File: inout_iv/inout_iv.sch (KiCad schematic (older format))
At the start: 1 part, among them P1 DIN_41612_128P

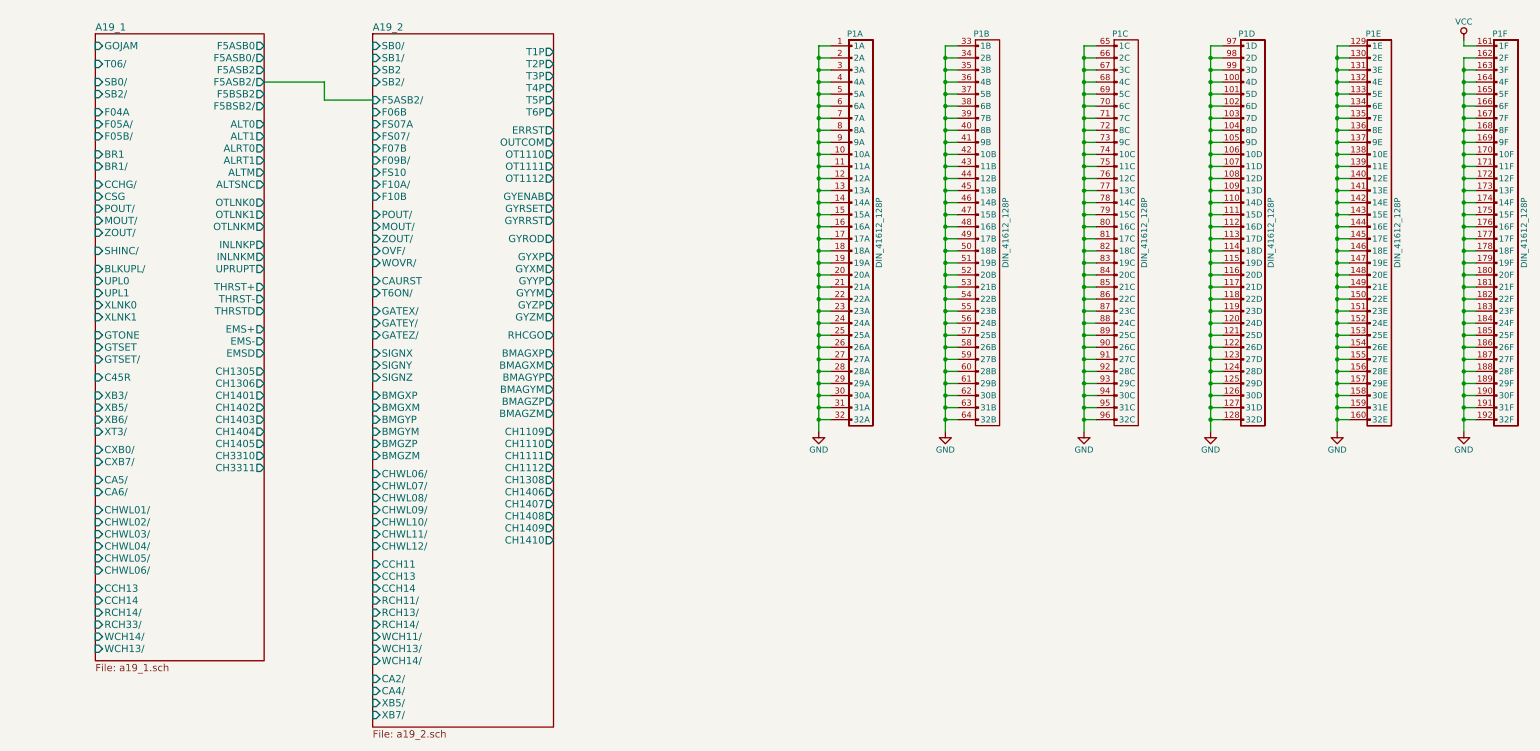
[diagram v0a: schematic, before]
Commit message: Tied in Inout IV and renamed MONPCH to the original MON+CH
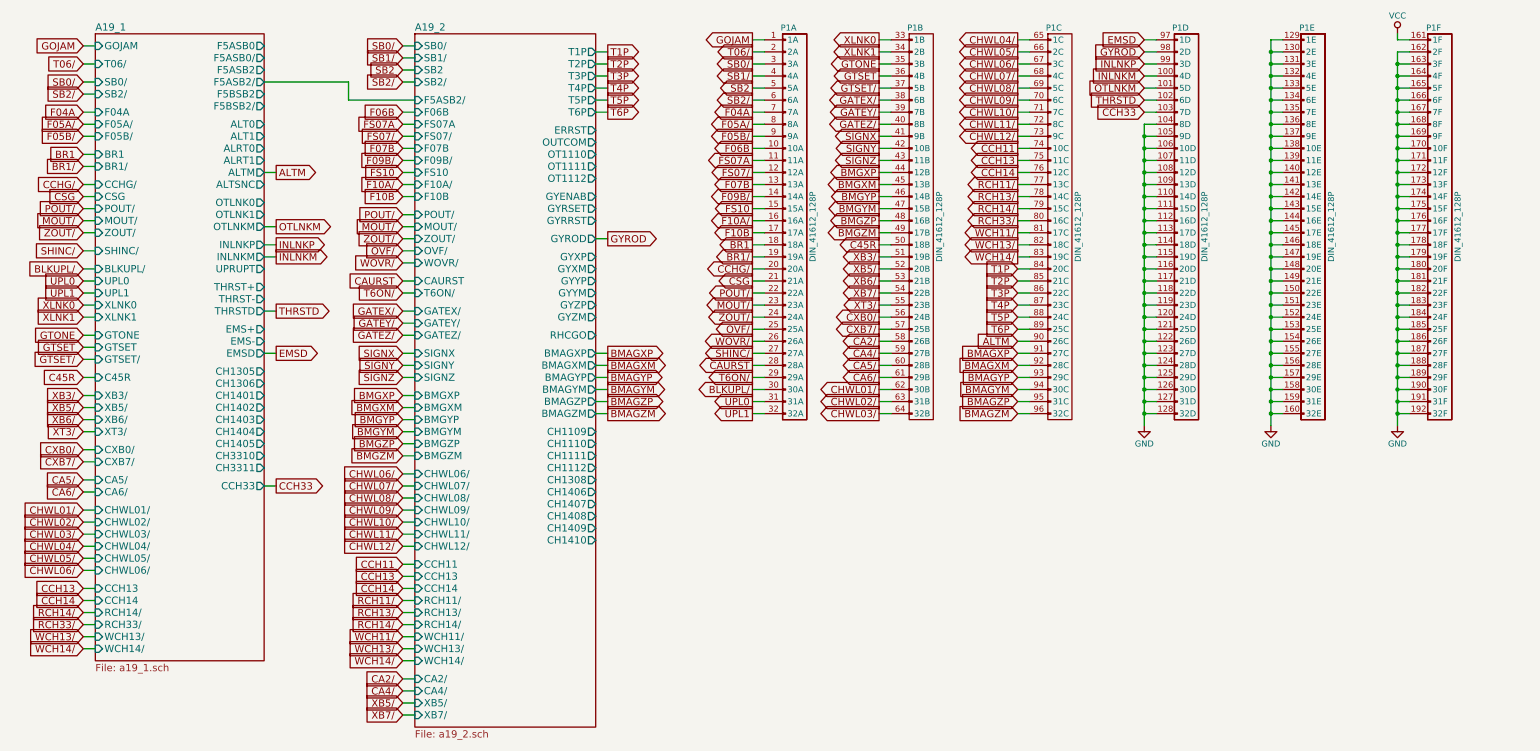
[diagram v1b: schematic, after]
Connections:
- net GND: no longer P1.1 (1A), P1.10 (10A), P1.100 (4D), P1.101 (5D), P1.102 (6D), P1.103 (7D), P1.11 (11A), P1.12 (12A), P1.13 (13A), P1.14 (14A), P1.15 (15A), P1.16 (16A), P1.17 (17A), P1.18 (18A), P1.19 (19A), P1.2 (2A), P1.20 (20A), P1.21 (21A), P1.22 (22A), P1.23 (23A), P1.24 (24A), P1.25 (25A), P1.26 (26A), P1.27 (27A), P1.28 (28A), P1.29 (29A), P1.3 (3A), P1.30 (30A), P1.31 (31A), P1.32 (32A), P1.33 (1B), P1.34 (2B), P1.35 (3B), P1.36 (4B), P1.37 (5B), P1.38 (6B), P1.39 (7B), P1.4 (4A), P1.40 (8B), P1.41 (9B), P1.42 (10B), P1.43 (11B), P1.44 (12B), P1.45 (13B), P1.46 (14B), P1.47 (15B), P1.48 (16B), P1.49 (17B), P1.5 (5A), P1.50 (18B), P1.51 (19B), P1.52 (20B), P1.53 (21B), P1.54 (22B), P1.55 (23B), P1.56 (24B), P1.57 (25B), P1.58 (26B), P1.59 (27B), P1.6 (6A), P1.60 (28B), P1.61 (29B), P1.62 (30B), P1.63 (31B), P1.64 (32B), P1.65 (1C), P1.66 (2C), P1.67 (3C), P1.68 (4C), P1.69 (5C), P1.7 (7A), P1.70 (6C), P1.71 (7C), P1.72 (8C), P1.73 (9C), P1.74 (10C), P1.75 (11C), P1.76 (12C), P1.77 (13C), P1.78 (14C), P1.79 (15C), P1.8 (8A), P1.80 (16C), P1.81 (17C), P1.82 (18C), P1.83 (19C), P1.84 (20C), P1.85 (21C), P1.86 (22C), P1.87 (23C), P1.88 (24C), P1.89 (25C), P1.9 (9A), P1.90 (26C), P1.91 (27C), P1.92 (28C), P1.93 (29C), P1.94 (30C), P1.95 (31C), P1.96 (32C), P1.97 (1D), P1.98 (2D), P1.99 (3D)
- new net ALTM: P1.90 (26C)
- new net BLKUPL/: P1.30 (30A)
- new net BMAGXM: P1.92 (28C)
- new net BMAGXP: P1.91 (27C)
- new net BMAGYM: P1.94 (30C)
- new net BMAGYP: P1.93 (29C)
- new net BMAGZM: P1.96 (32C)
- new net BMAGZP: P1.95 (31C)
- new net BMGXM: P1.45 (13B)
- new net BMGXP: P1.44 (12B)
- new net BMGYM: P1.47 (15B)
- new net BMGYP: P1.46 (14B)
- new net BMGZM: P1.49 (17B)
- new net BMGZP: P1.48 (16B)
- new net BR1: P1.18 (18A)
- new net BR1/: P1.19 (19A)
- new net C45R: P1.50 (18B)
- new net CA2/: P1.58 (26B)
- new net CA4/: P1.59 (27B)
- new net CA5/: P1.60 (28B)
- new net CA6/: P1.61 (29B)
- new net CAURST: P1.28 (28A)
- new net CCH11: P1.74 (10C)
- new net CCH13: P1.75 (11C)
- new net CCH14: P1.76 (12C)
- new net CCH33: P1.103 (7D)
- new net CCHG/: P1.20 (20A)
- new net CHWL01/: P1.62 (30B)
- new net CHWL02/: P1.63 (31B)
- new net CHWL03/: P1.64 (32B)
- new net CHWL04/: P1.65 (1C)
- new net CHWL05/: P1.66 (2C)
- new net CHWL06/: P1.67 (3C)
- new net CHWL07/: P1.68 (4C)
- new net CHWL08/: P1.69 (5C)
- new net CHWL09/: P1.70 (6C)
- new net CHWL10/: P1.71 (7C)
- new net CHWL11/: P1.72 (8C)
- new net CHWL12/: P1.73 (9C)
- new net CSG: P1.21 (21A)
- new net CXB0/: P1.56 (24B)
- new net CXB7/: P1.57 (25B)
- new net EMSD: P1.97 (1D)
- new net F04A: P1.7 (7A)
- new net F05A/: P1.8 (8A)
- new net F05B/: P1.9 (9A)
- new net F06B: P1.10 (10A)
- new net F07B: P1.13 (13A)
- new net F09B/: P1.14 (14A)
- new net F10A/: P1.16 (16A)
- new net F10B: P1.17 (17A)
- new net FS07/: P1.12 (12A)
- new net FS07A: P1.11 (11A)
- new net FS10: P1.15 (15A)
- new net GATEX/: P1.38 (6B)
- new net GATEY/: P1.39 (7B)
- new net GATEZ/: P1.40 (8B)
- new net GOJAM: P1.1 (1A)
- new net GTONE: P1.35 (3B)
- new net GTSET: P1.36 (4B)
- new net GTSET/: P1.37 (5B)
- new net GYROD: P1.98 (2D)
- new net INLNKM: P1.100 (4D)
- new net INLNKP: P1.99 (3D)
- new net MOUT/: P1.23 (23A)
- new net OTLNKM: P1.101 (5D)
- new net OVF/: P1.25 (25A)
- new net POUT/: P1.22 (22A)
- new net RCH11/: P1.77 (13C)
- new net RCH13/: P1.78 (14C)
- new net RCH14/: P1.79 (15C)
- new net RCH33/: P1.80 (16C)
- new net SB0/: P1.3 (3A)
- new net SB1/: P1.4 (4A)
- new net SB2: P1.5 (5A)
- new net SB2/: P1.6 (6A)
- new net SHINC/: P1.27 (27A)
- new net SIGNX: P1.41 (9B)
- new net SIGNY: P1.42 (10B)
- new net SIGNZ: P1.43 (11B)
- new net T06/: P1.2 (2A)
- new net T1P: P1.84 (20C)
- new net T2P: P1.85 (21C)
- new net T3P: P1.86 (22C)
- new net T4P: P1.87 (23C)
- new net T5P: P1.88 (24C)
- new net T6ON/: P1.29 (29A)
- new net T6P: P1.89 (25C)
- new net THRSTD: P1.102 (6D)
- new net UPL0: P1.31 (31A)
- new net UPL1: P1.32 (32A)
- new net WCH11/: P1.81 (17C)
- new net WCH13/: P1.82 (18C)
- new net WCH14/: P1.83 (19C)
- new net WOVR/: P1.26 (26A)
- new net XB3/: P1.51 (19B)
- new net XB5/: P1.52 (20B)
- new net XB6/: P1.53 (21B)
- new net XB7/: P1.54 (22B)
- new net XLNK0: P1.33 (1B)
- new net XLNK1: P1.34 (2B)
- new net XT3/: P1.55 (23B)
- new net ZOUT/: P1.24 (24A)
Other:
- moved on the sheet: P1A, P1B, P1C, P1D, P1E, P1F

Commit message: Tied in Inout II.
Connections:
- net GND: no longer P1.104 (8D), P1.105 (9D), P1.106 (10D), P1.107 (11D), P1.108 (12D), P1.109 (13D), P1.110 (14D), P1.111 (15D), P1.112 (16D), P1.113 (17D), P1.114 (18D), P1.115 (19D), P1.116 (20D), P1.117 (21D)
- new net CH1305: P1.104 (8D)
- new net CH1306: P1.105 (9D)
- new net CH1308: P1.106 (10D)
- new net CH1401: P1.107 (11D)
- new net CH1402: P1.108 (12D)
- new net CH1403: P1.109 (13D)
- new net CH1404: P1.110 (14D)
- new net CH1405: P1.111 (15D)
- new net CH1406: P1.112 (16D)
- new net CH1407: P1.113 (17D)
- new net CH1408: P1.114 (18D)
- new net CH1409: P1.115 (19D)
- new net CH1410: P1.116 (20D)
- new net CH3310: P1.117 (21D)
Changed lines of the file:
@@
 $EndComp
-Wire Wire Line
-	10500 1950 10600 1950
-Wire Wire Line
-	10500 2050 10600 2050
-Connection ~ 10500 2050
-Wire Wire Line
-	10500 2150 10600 2150
-Connection ~ 10500 2150
-Wire Wire Line
-	10500 2250 10600 2250
-Connection ~ 10500 2250
-Wire Wire Line
-	10500 2350 10600 2350
-Connection ~ 10500 2350
-Wire Wire Line
-	10500 2450 10600 2450
-Connection ~ 10500 2450
-Wire Wire Line
-	10500 2550 10600 2550
-Connection ~ 10500 2550
-Wire Wire Line
-	10500 2650 10600 2650
-Connection ~ 10500 2650
-Wire Wire Line
-	10500 2750 10600 2750
-Connection ~ 10500 2750
-Wire Wire Line
-	10500 2850 10600 2850
-Connection ~ 10500 2850
-Wire Wire Line
-	10500 2950 10600 2950
-Connection ~ 10500 2950
-Wire Wire Line
-	10500 3050 10600 3050
-Connection ~ 10500 3050
-Wire Wire Line
-	10500 3150 10600 3150
-Connection ~ 10500 3150
-Wire Wire Line
-	10500 3250 10600 3250
-Connection ~ 10500 3250
-Wire Wire Line
-	10500 3350 10600 3350
-Connection ~ 10500 3350
-Wire Wire Line
-	10500 3450 10600 3450
-Connection ~ 10500 3450
-Wire Wire Line
-	10500 3550 10600 3550
-Connection ~ 10500 3550
-Wire Wire Line
-	10500 3650 10600 3650
-Connection ~ 10500 3650
-Wire Wire Line
-	10500 3750 10600 3750
-Connection ~ 10500 3750
-Wire Wire Line
-	10500 3850 10600 3850
-Connection ~ 10500 3850
-Wire Wire Line
-	10500 3950 10600 3950
-Connection ~ 10500 3950
 Wire Wire Line
 	10500 4050 10600 4050
@@
 THRSTD
 Wire Wire Line
-	10500 1950 10500 4450
-Wire Wire Line
 	10600 1750 10500 1750
 Text GLabel 10500 1750 0    60   Input ~ 0
 THRSTD
+Wire Wire Line
+	3200 4000 3300 4000
+Text GLabel 3300 4000 2    60   Output ~ 0
+CH1305
+Wire Wire Line
+	3200 4100 3300 4100
+Text GLabel 3300 4100 2    60   Output ~ 0
+CH1306
+Wire Wire Line
+	3200 4200 3300 4200
+Text GLabel 3300 4200 2    60   Output ~ 0
+CH1401
+Wire Wire Line
+	3200 4300 3300 4300
+Text GLabel 3300 4300 2    60   Output ~ 0
+CH1402
+Wire Wire Line
+	3200 4400 3300 4400
+Text GLabel 3300 4400 2    60   Output ~ 0
+CH1403
+Wire Wire Line
+	3200 4500 3300 4500
+Text GLabel 3300 4500 2    60   Output ~ 0
+CH1404
+Wire Wire Line
+	3200 4600 3300 4600
+Text GLabel 3300 4600 2    60   Output ~ 0
+CH1405
+Wire Wire Line
+	3200 4700 3300 4700
+Text GLabel 3300 4700 2    60   Output ~ 0
+CH3310
+Wire Wire Line
+	5950 4900 6050 4900
+Text GLabel 6050 4900 2    60   Output ~ 0
+CH1308
+Wire Wire Line
+	5950 5000 6050 5000
+Text GLabel 6050 5000 2    60   Output ~ 0
+CH1406
+Wire Wire Line
+	5950 5100 6050 5100
+Text GLabel 6050 5100 2    60   Output ~ 0
+CH1407
+Wire Wire Line
+	5950 5200 6050 5200
+Text GLabel 6050 5200 2    60   Output ~ 0
+CH1408
+Wire Wire Line
+	5950 5300 6050 5300
+Text GLabel 6050 5300 2    60   Output ~ 0
+CH1409
+Wire Wire Line
+	5950 5400 6050 5400
+Text GLabel 6050 5400 2    60   Output ~ 0
+CH1410
+Wire Wire Line
+	10600 1950 10500 1950
+Text GLabel 10500 1950 0    60   Input ~ 0
+CH1305
+Wire Wire Line
+	10600 2050 10500 2050
+Text GLabel 10500 2050 0    60   Input ~ 0
+CH1306
+Wire Wire Line
+	10600 2250 10500 2250
+Text GLabel 10500 2250 0    60   Input ~ 0
+CH1401
+Wire Wire Line
+	10600 2350 10500 2350
+Text GLabel 10500 2350 0    60   Input ~ 0
+CH1402
+Wire Wire Line
+	10600 2450 10500 2450
+Text GLabel 10500 2450 0    60   Input ~ 0
+CH1403
+Wire Wire Line
+	10600 2550 10500 2550
+Text GLabel 10500 2550 0    60   Input ~ 0
+CH1404
+Wire Wire Line
+	10600 2650 10500 2650
+Text GLabel 10500 2650 0    60   Input ~ 0
+CH1405
+Wire Wire Line
+	10600 3250 10500 3250
+Text GLabel 10500 3250 0    60   Input ~ 0
+CH3310
+Wire Wire Line
+	10600 2150 10500 2150
+Text GLabel 10500 2150 0    60   Input ~ 0
+CH1308
+Wire Wire Line
+	10600 2750 10500 2750
+Text GLabel 10500 2750 0    60   Input ~ 0
+CH1406
+Wire Wire Line
+	10600 2850 10500 2850
+Text GLabel 10500 2850 0    60   Input ~ 0
+CH1407
+Wire Wire Line
+	10600 2950 10500 2950
+Text GLabel 10500 2950 0    60   Input ~ 0
+CH1408
+Wire Wire Line
+	10600 3050 10500 3050
+Text GLabel 10500 3050 0    60   Input ~ 0
+CH1409
+Wire Wire Line
+	10600 3150 10500 3150
+Text GLabel 10500 3150 0    60   Input ~ 0
+CH1410
+Wire Wire Line
+	10500 3650 10600 3650
+Connection ~ 10500 3650
+Wire Wire Line
+	10500 3750 10600 3750
+Connection ~ 10500 3750
+Wire Wire Line
+	10500 3850 10600 3850
+Connection ~ 10500 3850
+Wire Wire Line
+	10500 3950 10600 3950
+Connection ~ 10500 3950
+Wire Wire Line
+	10500 3450 10600 3450
+Connection ~ 10500 3450
+Wire Wire Line
+	10500 3550 10600 3550
+Connection ~ 10500 3550
+Wire Wire Line
+	10600 3350 10500 3350
+Wire Wire Line
+	10500 3350 10500 4450
 $EndSCHEMATC

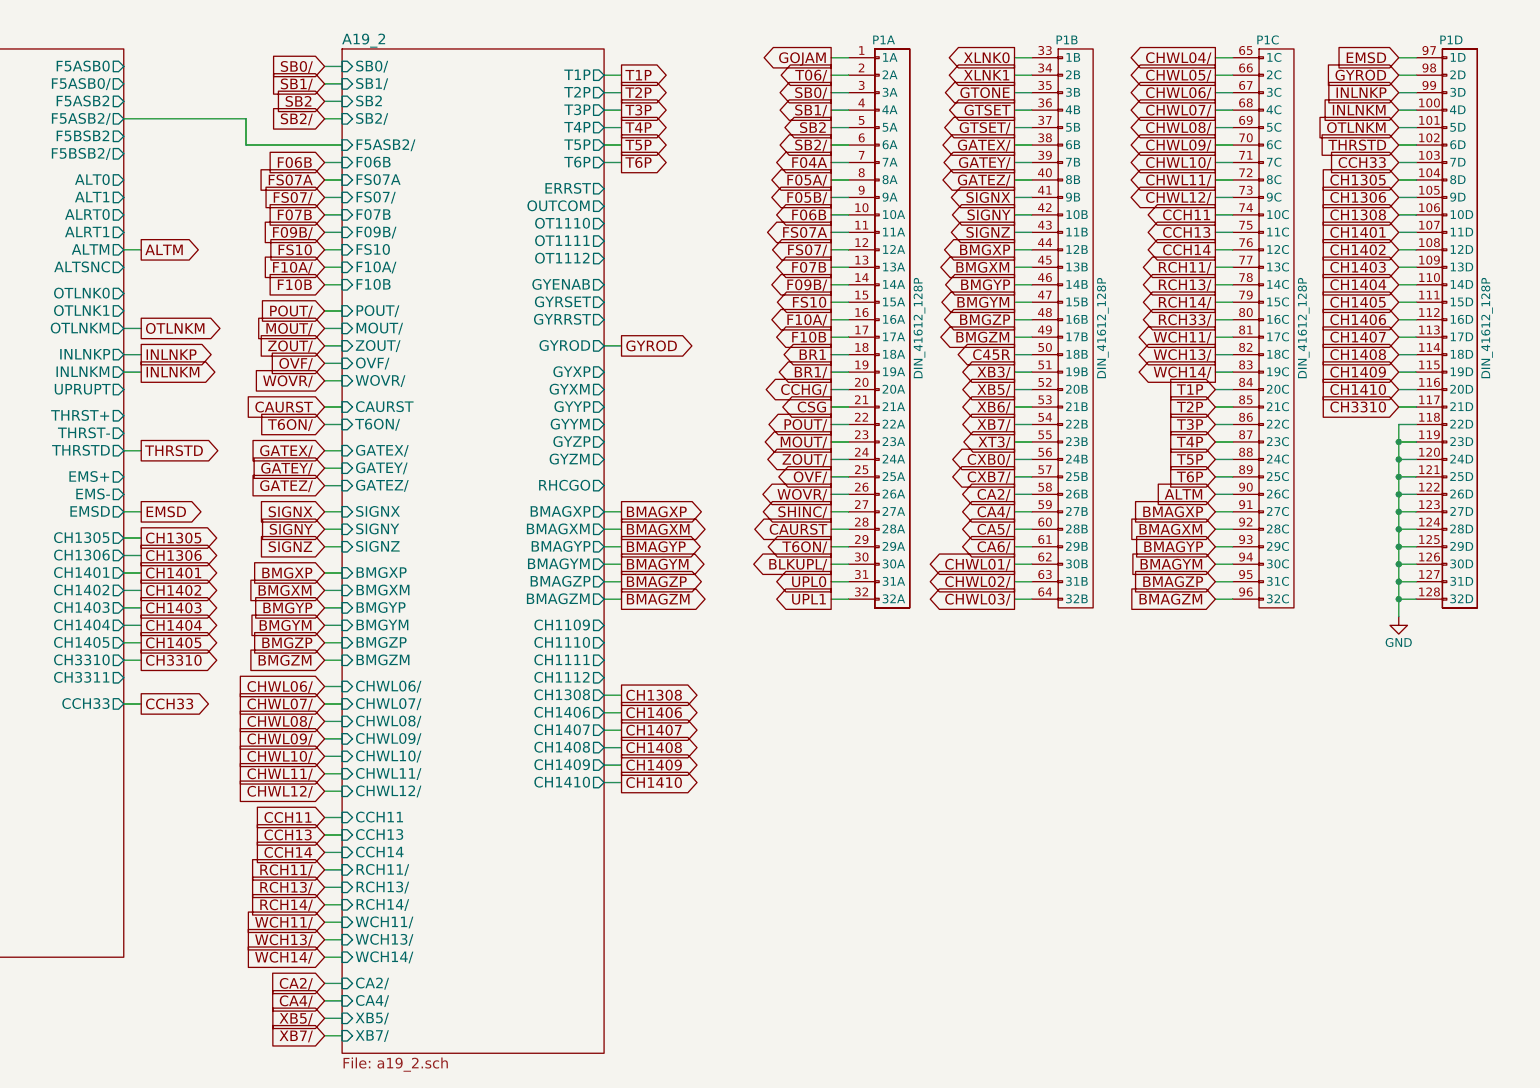
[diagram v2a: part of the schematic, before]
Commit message: Added most of the rest of Inout III and tied it in. Still not sure where to put the downlink stuff, standby, and CHOR propers.
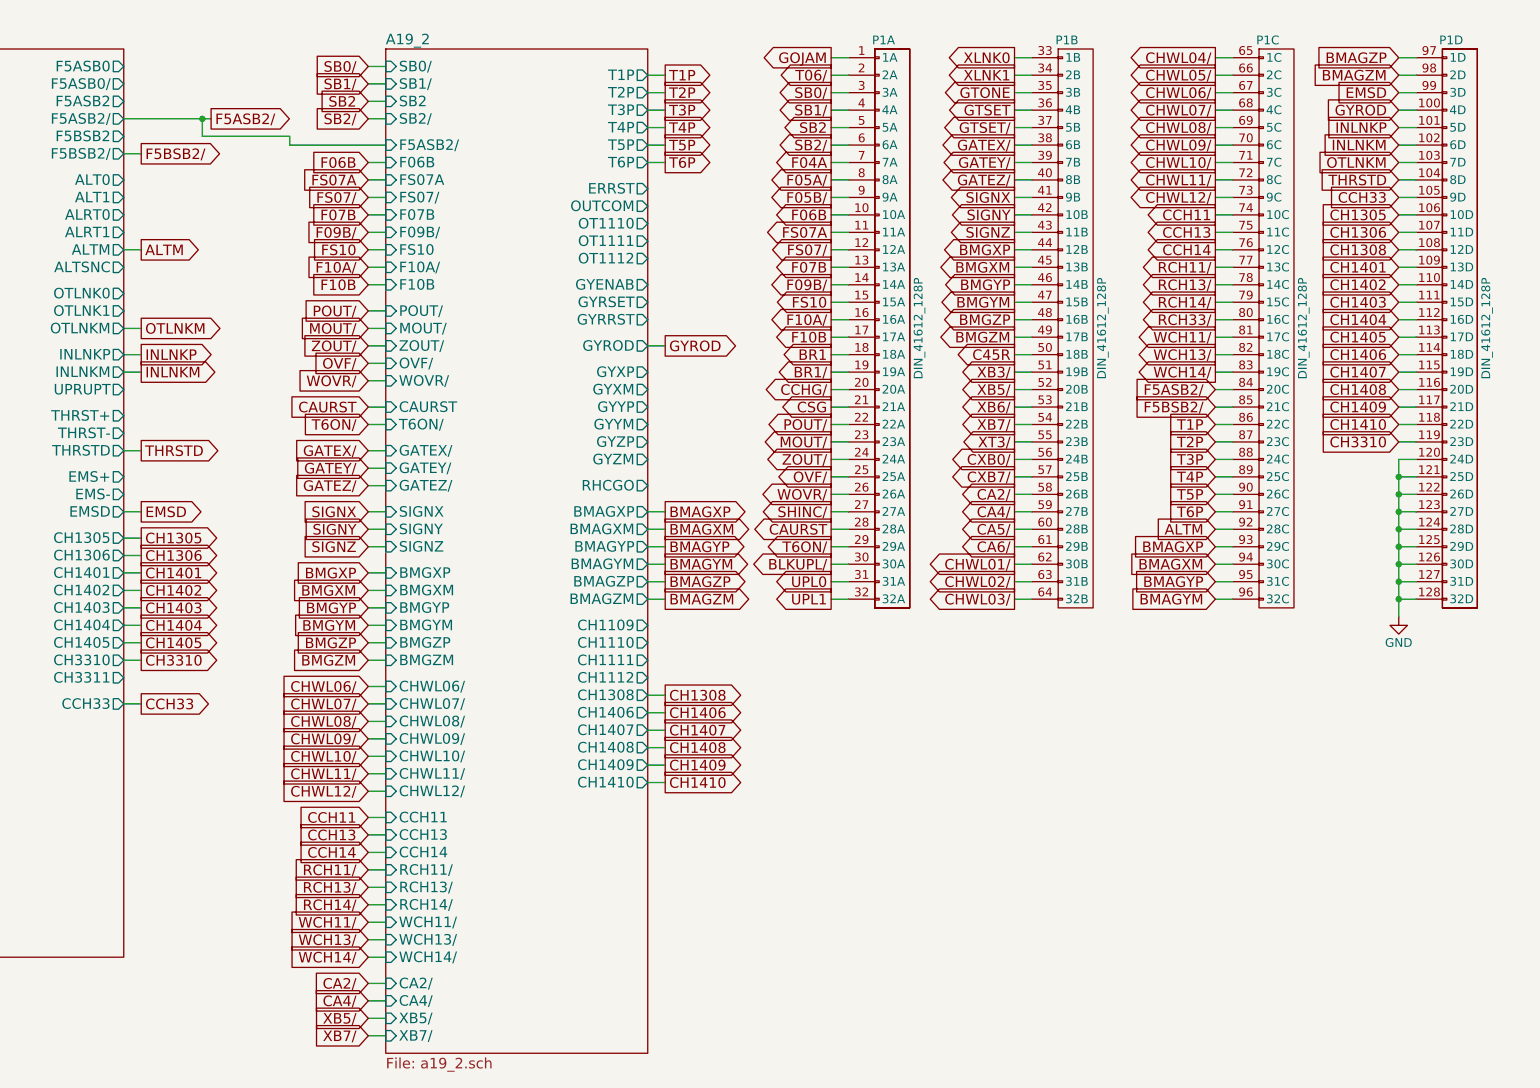
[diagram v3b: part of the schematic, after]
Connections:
- net ALTM: now also P1.92 (28C); no longer P1.90 (26C)
- net BMAGXM: now also P1.94 (30C); no longer P1.92 (28C)
- net BMAGXP: now also P1.93 (29C); no longer P1.91 (27C)
- net BMAGYM: now also P1.96 (32C); no longer P1.94 (30C)
- net BMAGYP: now also P1.95 (31C); no longer P1.93 (29C)
- net BMAGZM: now also P1.98 (2D); no longer P1.96 (32C)
- net BMAGZP: now also P1.97 (1D); no longer P1.95 (31C)
- net CCH33: now also P1.105 (9D); no longer P1.103 (7D)
- net CH1305: now also P1.106 (10D); no longer P1.104 (8D)
- net CH1306: now also P1.107 (11D); no longer P1.105 (9D)
- net CH1308: now also P1.108 (12D); no longer P1.106 (10D)
- net CH1401: now also P1.109 (13D); no longer P1.107 (11D)
- net CH1402: now also P1.110 (14D); no longer P1.108 (12D)
- net CH1403: now also P1.111 (15D); no longer P1.109 (13D)
- net CH1404: now also P1.112 (16D); no longer P1.110 (14D)
- net CH1405: now also P1.113 (17D); no longer P1.111 (15D)
- net CH1406: now also P1.114 (18D); no longer P1.112 (16D)
- net CH1407: now also P1.115 (19D); no longer P1.113 (17D)
- net CH1408: now also P1.116 (20D); no longer P1.114 (18D)
- net CH1409: now also P1.117 (21D); no longer P1.115 (19D)
- net CH1410: now also P1.118 (22D); no longer P1.116 (20D)
- net CH3310: now also P1.119 (23D); no longer P1.117 (21D)
- net EMSD: now also P1.99 (3D); no longer P1.97 (1D)
- net GND: no longer P1.118 (22D), P1.119 (23D)
- net GYROD: now also P1.100 (4D); no longer P1.98 (2D)
- net INLNKM: now also P1.102 (6D); no longer P1.100 (4D)
- net INLNKP: now also P1.101 (5D); no longer P1.99 (3D)
- net OTLNKM: now also P1.103 (7D); no longer P1.101 (5D)
- net T1P: now also P1.86 (22C); no longer P1.84 (20C)
- net T2P: now also P1.87 (23C); no longer P1.85 (21C)
- net T3P: now also P1.88 (24C); no longer P1.86 (22C)
- net T4P: now also P1.89 (25C); no longer P1.87 (23C)
- net T5P: now also P1.90 (26C); no longer P1.88 (24C)
- net T6P: now also P1.91 (27C); no longer P1.89 (25C)
- net THRSTD: now also P1.104 (8D); no longer P1.102 (6D)
- new net F5ASB2/: P1.84 (20C)
- new net F5BSB2/: P1.85 (21C)
